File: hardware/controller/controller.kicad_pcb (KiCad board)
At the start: 2 copper layers, 37.1 x 35.6 mm, 6 parts, among them J1 SENSOR_LINK_2mm, J4 USB_STACK_4_1.27mm, J5 USB2_PIGTAIL_4_WIRES, U2 ADS1115 module

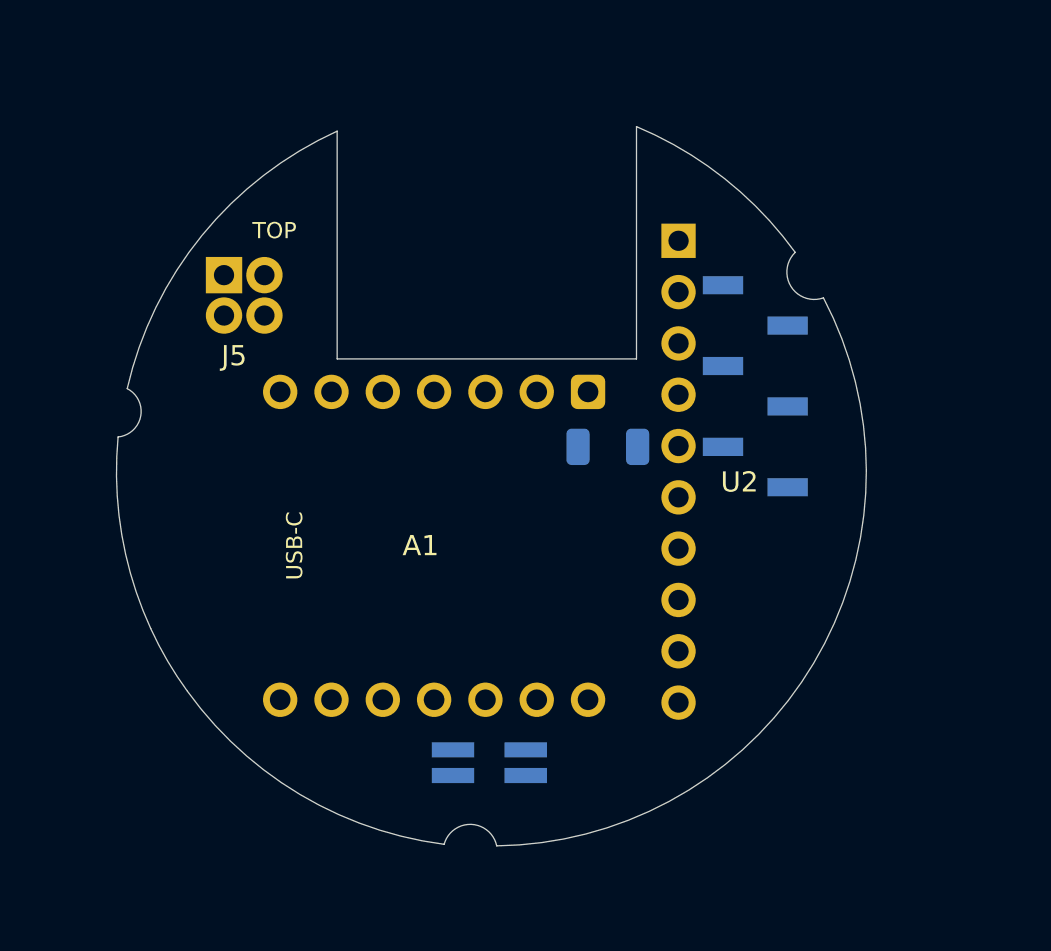
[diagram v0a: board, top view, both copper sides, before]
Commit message: Update 32 files (3D, docs, hardware, raíz)
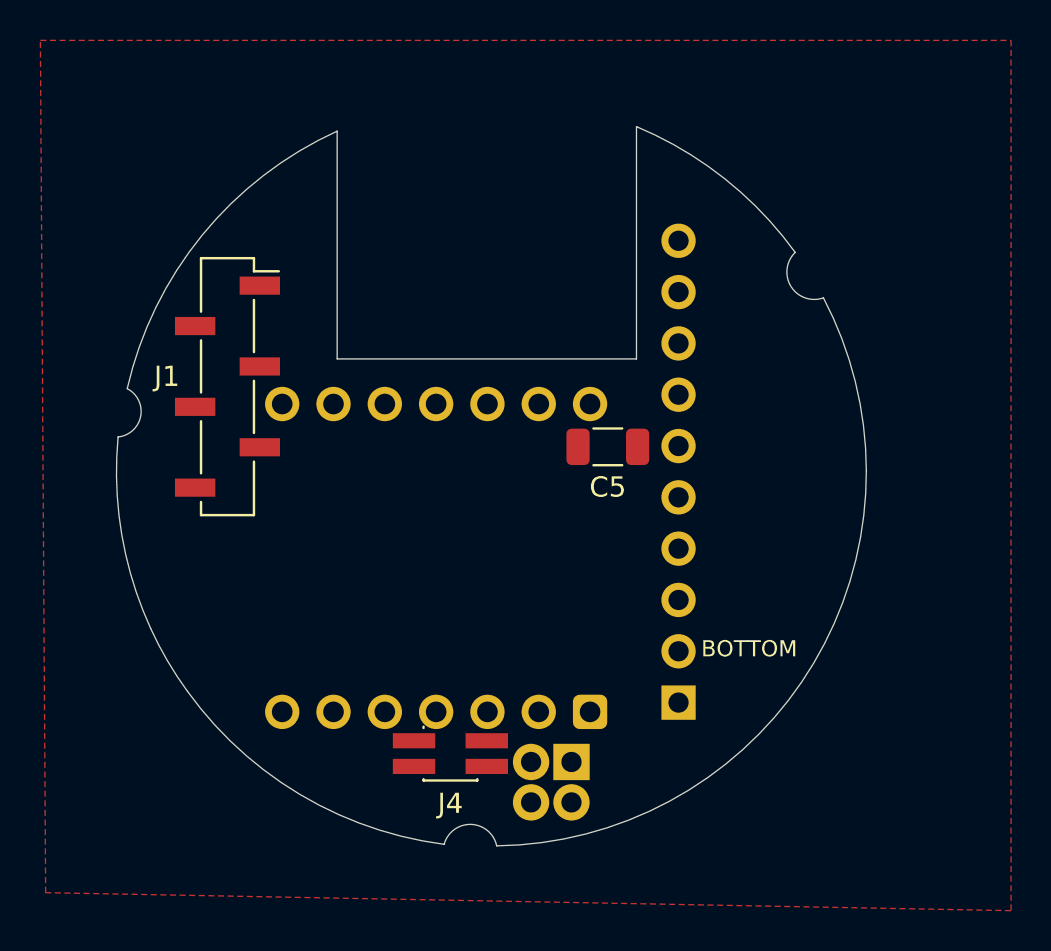
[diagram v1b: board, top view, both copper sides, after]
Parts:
- A1, J5, U2: moved to B.Cu
- C5, J1: moved to F.Cu
- J4: footprint Connector_PinSocket_1.27mm:PinSocket_2x02_P1.27mm_Vertical_SMD -> Turbimeter:USB_StackSocket_2x02_P1.27mm_Upper_v10; moved to F.Cu
- moved J5 29.6 mm to (38.2, 47.6), turned to 180 degrees
- moved J1 26.1 mm to (21.2, 29.0), turned to 0 degrees
- moved U2 22.9 mm to (43.5, 44.7), turned to 90 degrees
- moved J4 1.98 mm to (32.2, 47.2), turned to 0 degrees
- moved A1 0.61 mm to (31.5, 37.5), turned to 90 degrees
- turned C5 to 180 degrees
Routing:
- added copper zone on F.Cu, net /GND
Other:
- board text added: "F.Cu ONLY — SOLDER SIDE: SMD, ALL JOINTS AND ROUTING"
- board text added: "J1/J4 MATCH ROUTED BASE - KEEP MATING AXES"
- board text added: "UPPER: B = COMPONENTS UP / F = SOLDER + SMD"
- board text removed: "B.Cu ONLY — SOLDER SIDE: SMD, ALL JOINTS AND ROUTING"

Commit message: Update 9 files (hardware)
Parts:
- moved J5 2.32 mm to (37.9, 49.9), turned to 0 degrees
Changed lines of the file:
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@@
 	(footprint "Turbimeter:USB_Cable_WireHoles_2x02_P2mm"
 		(layer "B.Cu")
-		(at 38.2 47.6 180)
+		(at 37.93 49.9)
 		(descr "Design: Ing. Alex M. Rivera. Four direct wire holes: 1 VBUS, 2 GND, 3 D-, 4 D+. 2x2 P2mm; 1mm drill; bare wires enter TOP and solder BOTTOM. No connector body; strain relief required.")
 		(property "Reference" "J5"
@@
 		(attr through_hole)
 		(pad "1" thru_hole rect
-			(at 0 0 180)
+			(at 0 0)
 			(size 1.8 1.8)
 			(drill 1)
@@
 		)
 		(pad "2" thru_hole circle
-			(at 2 0 180)
+			(at 2 0)
 			(size 1.8 1.8)
 			(drill 1)
@@
 		)
 		(pad "3" thru_hole circle
-			(at 0 -2 180)
+			(at 0 -2)
 			(size 1.8 1.8)
 			(drill 1)
@@
 		)
 		(pad "4" thru_hole circle
-			(at 2 -2 180)
+			(at 2 -2)
 			(size 1.8 1.8)
 			(drill 1)
